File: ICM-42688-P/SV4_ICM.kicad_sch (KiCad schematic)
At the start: 15 parts, among them U1 SuperMini nRF52840, U2 ICM-42688-P, U3 MMC5983MA

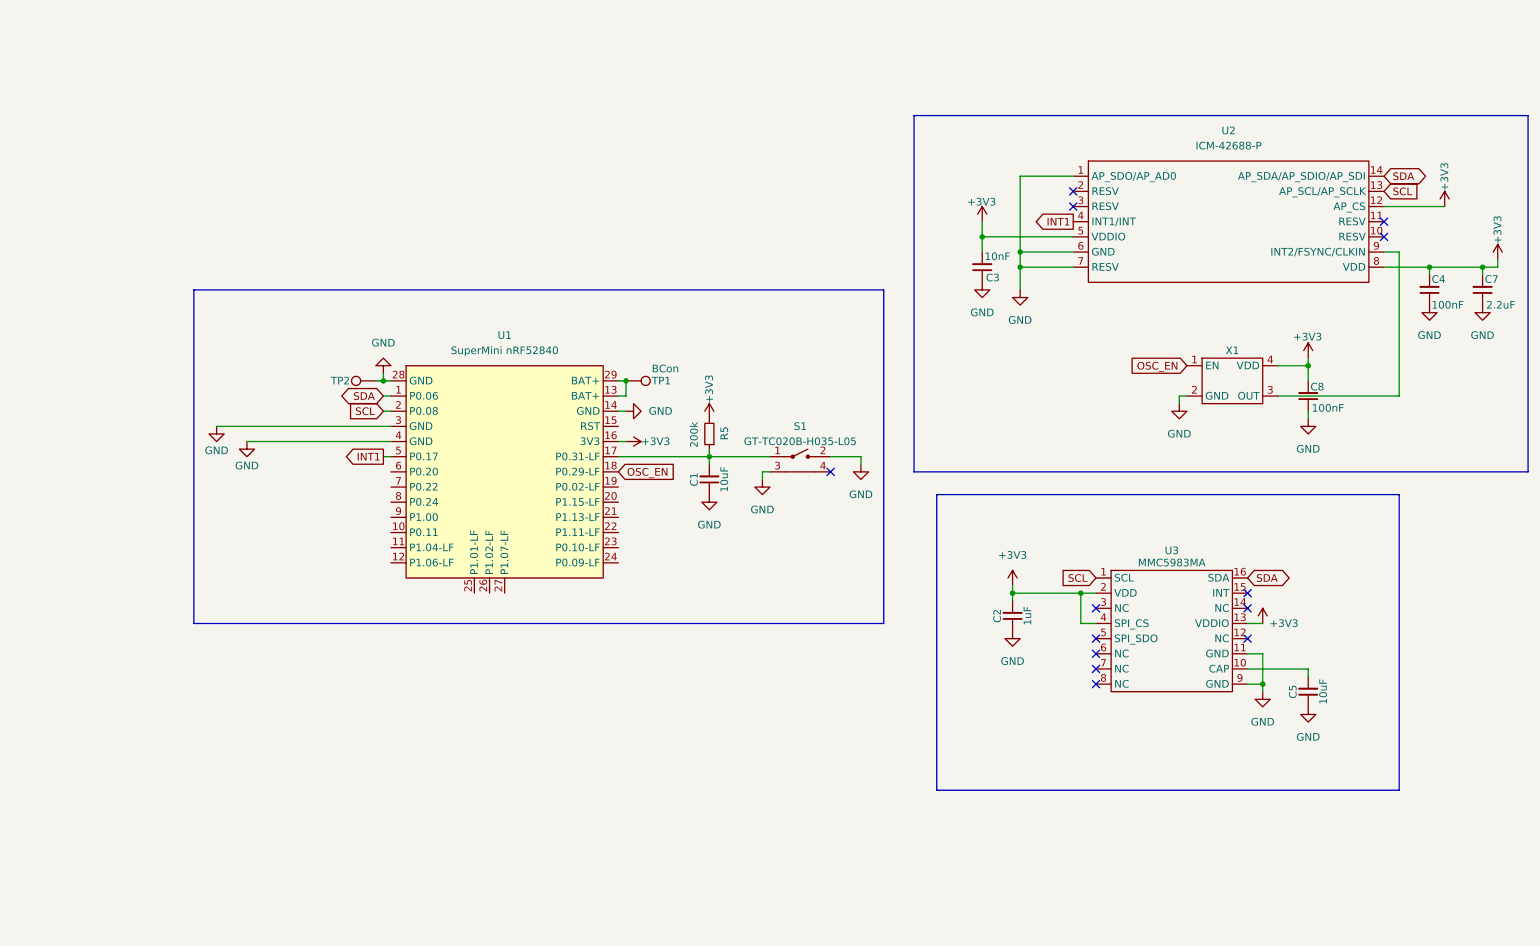
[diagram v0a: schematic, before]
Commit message: - Added PCB push hole for easier disassembly - Increased pin push hole for SIM tools - Added disassembly slide to release battery tray - Added i2c pullups... I can't believe I forgot those. I already ordered the boards, too. Am I stupid??? - Increased height of button deflector to direct forces more inward - Added "mirror" on PCB for better light - Added photos of tracker
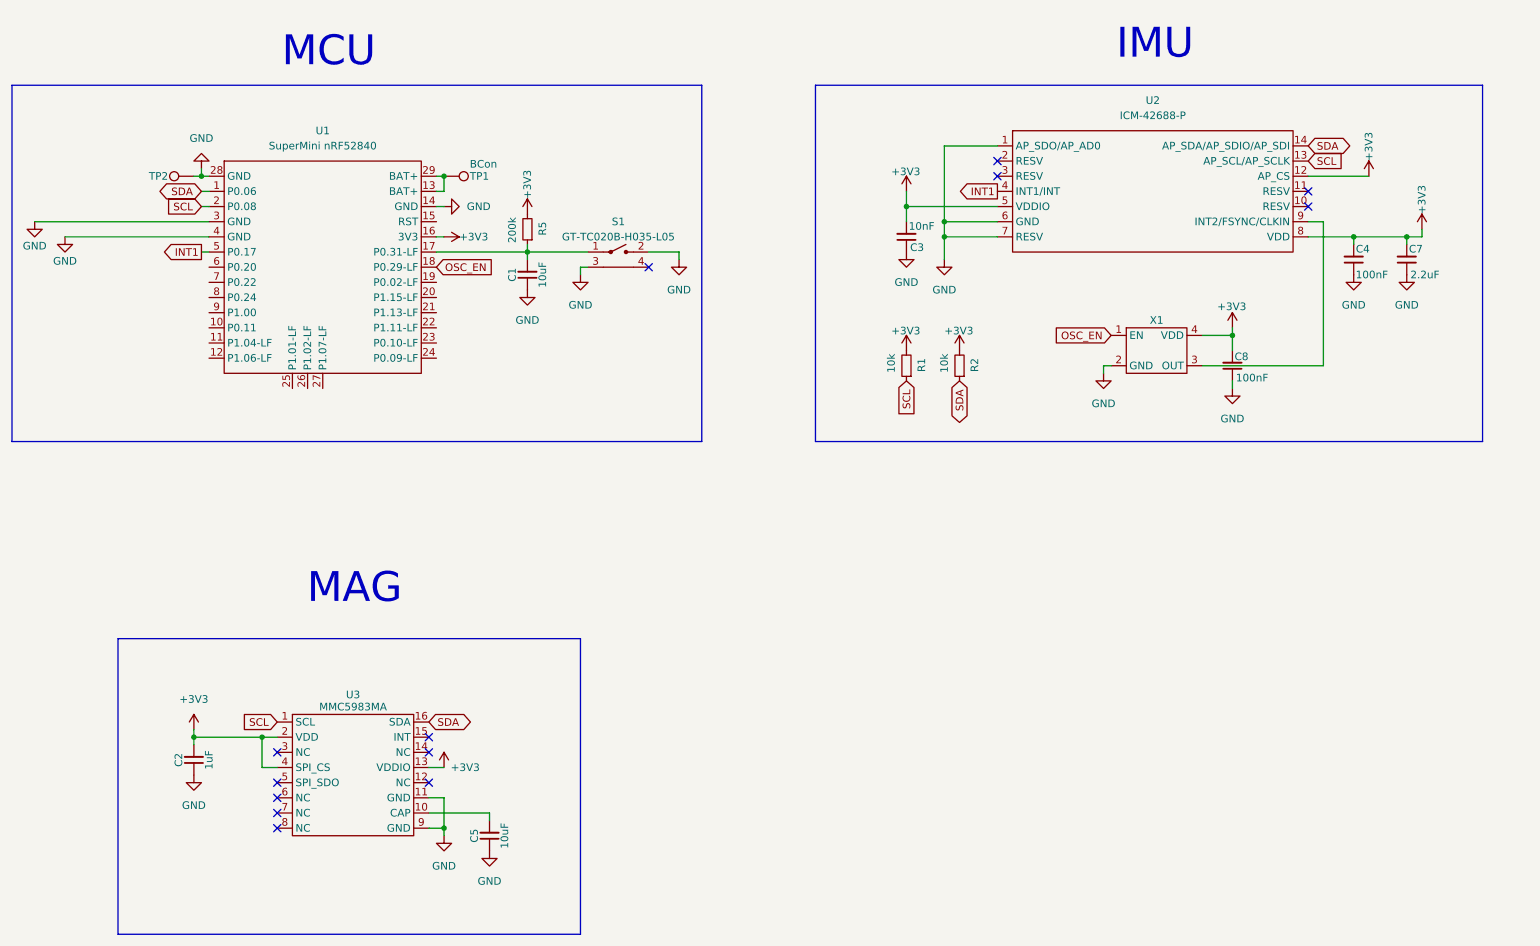
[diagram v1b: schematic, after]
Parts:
- added R1, R2: 10k, Resistor_SMD:R_0402_1005Metric, symbol LSM6DSV Symbols:R_Small
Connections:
- net +3V3: now also R1.2, R2.2
- net SCL: now also R1.1
- net SDA: now also R2.1
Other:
- note added: "IMU"
- note added: "MAG"
- note added: "MCU"
- company: (none) -> Macroplastics
- title: (none) -> Fuimini ICM
- moved on the sheet: C1, C2, C3, C4, C5, C7, C8, R5, S1, TP1, TP2, U2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

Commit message: Added supermini debug jig. Moved case button location to match PCB.
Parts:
- TP1, TP2: footprint justPads_custom:3_4-2.5_3.5 -> justPads_custom:2_4-1.5_3.5_1
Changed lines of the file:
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@@
 			)
 		)
-		(property "Footprint" "justPads_custom:3_4-2.5_3.5"
+		(property "Footprint" "justPads_custom:2_4-1.5_3.5_1"
 			(at 52.07 44.45 0)
 			(effects
@@
 			)
 		)
-		(property "Footprint" "justPads_custom:3_4-2.5_3.5"
+		(property "Footprint" "justPads_custom:2_4-1.5_3.5_1"
 			(at 93.98 54.61 0)
 			(effects

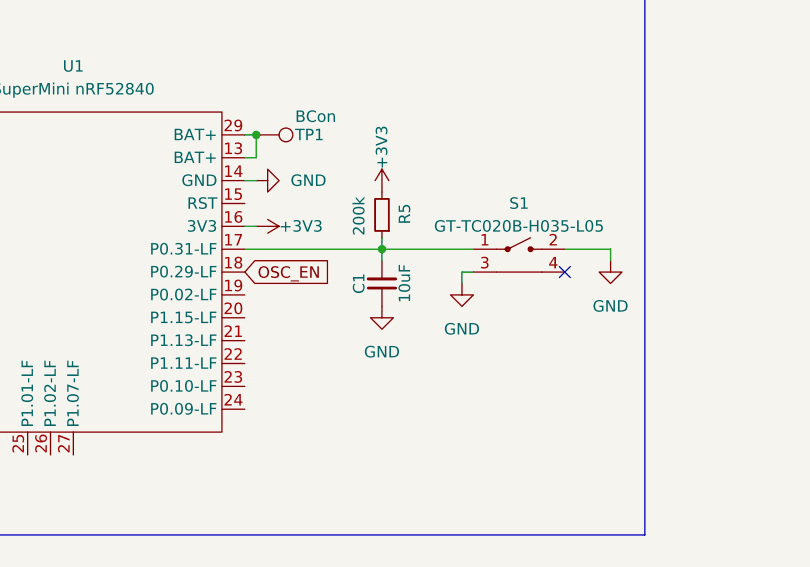
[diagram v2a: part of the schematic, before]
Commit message: - Added dimensions to dock pcb - some other stuff probably that i forgot to write down
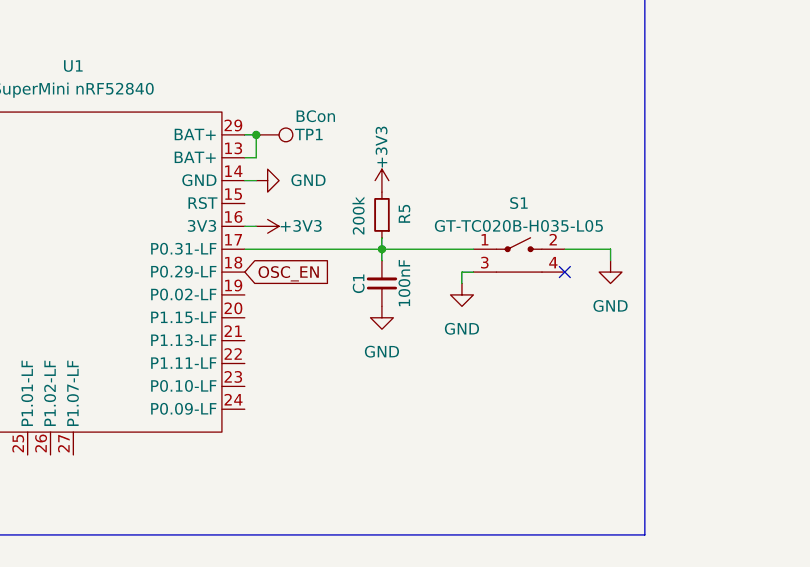
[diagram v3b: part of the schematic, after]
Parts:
- C1: value 10uF -> 100nF
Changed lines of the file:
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@@
 			)
 		)
-		(property "Value" "10uF"
+		(property "Value" "100nF"
 			(at 110.49 66.04 90)
 			(effects

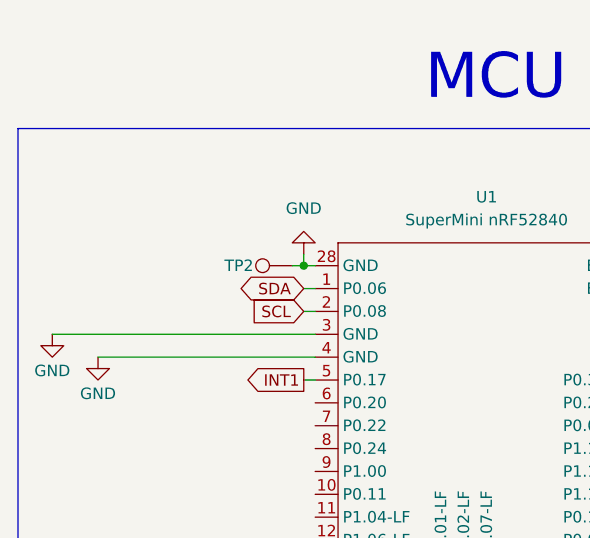
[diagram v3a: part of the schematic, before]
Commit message: - Added battery disconnect switch on PCB - Fixed dock dimension issues - Removed stl files from dock folder. Just split the step file in your slicer. - Added 3mf file for dock models. Compatible with Orca Slicer.
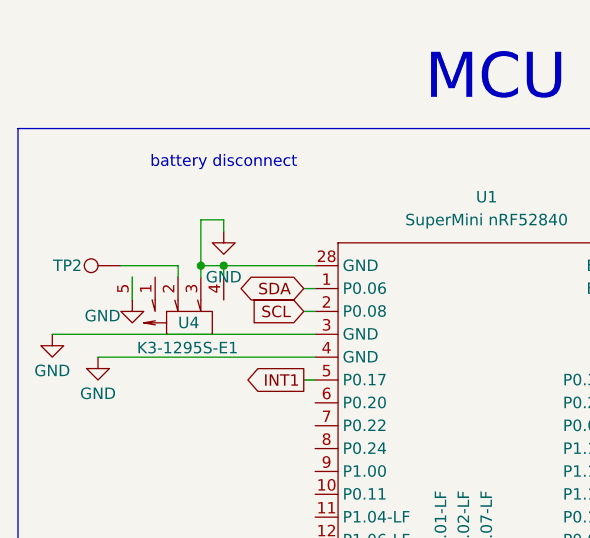
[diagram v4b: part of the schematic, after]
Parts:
- added U4: K3-1295S-E1, buttons_custom:K3-1295S-E1, symbol button_custom:K3-1295S-E1
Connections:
- net GND: now also U4.3, U4.4, U4.5; no longer TP2.1
- new net: TP2.1, U4.2
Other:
- note added: "battery disconnect"
- moved on the sheet: TP2
